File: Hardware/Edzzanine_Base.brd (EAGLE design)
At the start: 30.5 x 44.5 mm, 6 parts

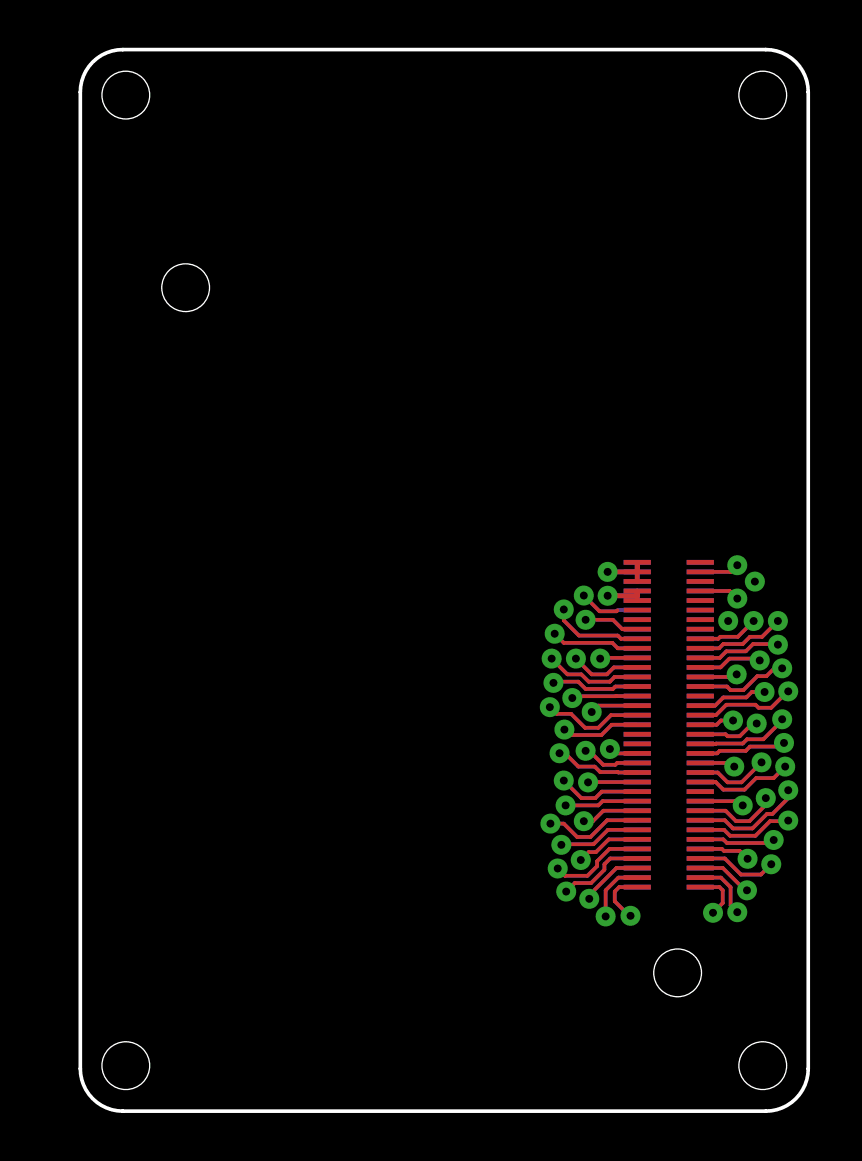
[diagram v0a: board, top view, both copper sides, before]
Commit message: completed base layout, ready for review.  Removed testing layouts and other noise
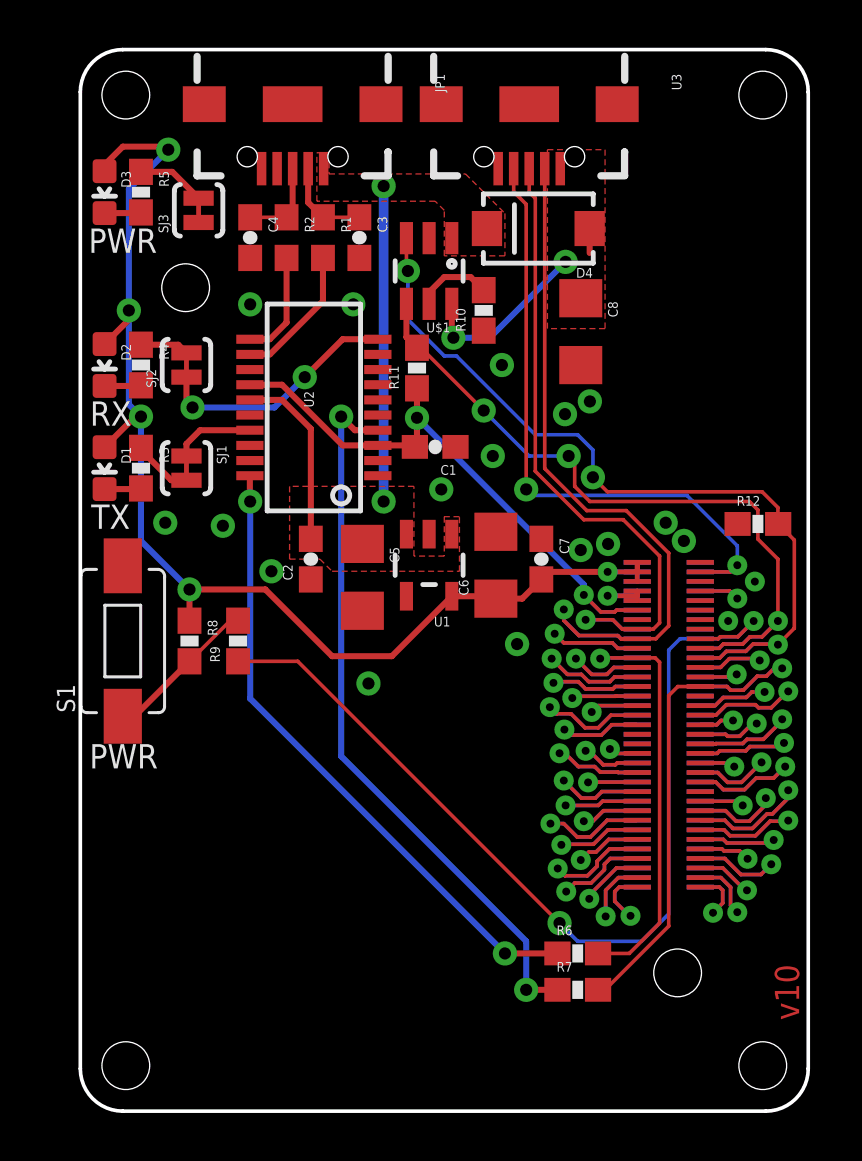
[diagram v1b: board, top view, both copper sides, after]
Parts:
- added C1, C2, C7: 0.1uF, SparkFun-Capacitors:0603-CAP
- added C3, C4: 47pF, SparkFun-Capacitors:0603-CAP
- added C5, C6, C8: 10uF, SparkFun-Capacitors:1206
- added D1: RED, SparkFun-LED:LED-0603
- added D2: YELLOW, SparkFun-LED:LED-0603
- added D3: BLUE, SparkFun-LED:LED-0603
- added D4: (no value), SparkFun-DiscreteSemi:SMA-DIODE
- added JP1: USB_MICROB, SparkFun-Connectors:USB-B-MICRO-SMD_V03
- added R1, R2: 27, SparkFun-Resistors:0603
- added R10: 287, SparkFun-Resistors:0603-RES
- added R11, R8: 10K, SparkFun-Resistors:0603-RES
- added R12: 100k, SparkFun-Resistors:0603-RES
- added R3, R4, R5: 1K, SparkFun-Resistors:0603-RES
- added R6, R7: 100, SparkFun-Resistors:0603-RES
- added R9: 22, SparkFun-Resistors:0603-RES
- added S1: POWER, SparkFun-Electromechanical:TACTILE-SWITCH-1101NE
- added SJ1, SJ2, SJ3: JUMPER-PAD-2-NC_BY_TRACE, SparkFun-Passives:PAD-JUMPER-2-NC_BY_TRACE_YES_SILK
- added U$1: MIC2039, Testing:SOT23-6
- added U1: MIC5219 3.3V, SparkFun-PowerIC:SOT23-5
- added U2: FTS31XS-U, SparkFun-DigitalIC:SSOP20_L
- added U3: (no value), SparkFun-Connectors:USB-AB-MICRO-SMD_V03
- renumbered U$2 to E1
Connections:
- new net 5V: C2.2, C5.1, D4.C, JP1.VBUS1, U$1.1, U1.1, U1.3, U2.15
- new net N$1: SJ1.1, U2.17
- new net N$10: D2.C, R4.2
- new net N$11: R6.1, U2.20
- new net N$12: D3.C, R5.2
- new net N$13: R5.1, SJ3.2
- new net N$14: R7.1, U2.4
- new net N$15: R8.2, R9.2, S1.P$1
- new net N$16: R10.2, U$1.5
- new net N$18: C8.1, D4.A, U$1.6, U3.VBUS1
- new net N$2: C3.1, JP1.D-1, R1.1
- new net N$3: C4.1, JP1.D+1, R2.1
- new net N$4: R1.2, U2.12
- new net N$5: R2.2, U2.11
- new net N$6: SJ2.1, U2.10
- new net N$7: R3.1, SJ1.2
- new net N$8: R4.1, SJ2.2
- new net N$9: D1.C, R3.2
- net 1.8V: now also C1.2, R11.1, U2.14, U2.3
- net FAULT: now also R11.2, U$1.4
- net GND: now also C1.1, C2.1, C3.2, C4.2, C5.2, C6.2, C7.1, C8.2, JP1.GND1, JP1.SHIELD1, JP1.SHIELD2, JP1.SHIELD3, R10.1, R12.1, S1.P$2, SJ3.1, U$1.2, U1.2, U2.16, U2.6, U3.GND1
- net GP134_UART_2_RX: now also R6.2
- net GP135_UART_2_TX: now also R7.2
- net PSW: now also R12.2, U$1.3
- net PWRBTN#: now also R9.1
- net USB_DN: now also U3.D-1
- net USB_DP: now also U3.D+1
- net USB_ID: now also U3.ID1
- net VSYS: now also C6.1, C7.2, D1.A, D2.A, D3.A, R8.1, U1.5
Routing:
- net VSYS: track 4.48 -> 53.3 mm, vias 1 -> 5
- net PWRBTN#: track 5.08 -> 41.3 mm, vias 1 -> 2
- net N$14: track 0.00 -> 30.3 mm, vias 0 -> 2
- net PSW: track 7.00 -> 36.2 mm, vias 1 -> 3
- net N$11: track 0.00 -> 26.6 mm, vias 0 -> 2
- net FAULT: track 7.45 -> 32.1 mm, vias 1 -> 3
- net USB_ID: track 3.33 -> 27.6 mm, vias 1 -> 2
- net USB_DN: track 7.70 -> 31.5 mm
- net USB_DP: track 4.65 -> 27.9 mm
- net 1.8V: track 4.25 -> 25.9 mm, vias 1 -> 2
- net 5V: track 0.00 -> 20.9 mm, vias 0 -> 2
- net GP135_UART_2_TX: track 7.74 -> 22.9 mm
- net GP134_UART_2_RX: track 3.13 -> 18.2 mm
- net N$6: track 0.00 -> 10.3 mm, vias 0 -> 2
- net N$18: track 0.00 -> 8.49 mm, vias 0 -> 2
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- added copper zone on layer 1, net 5V
- added copper zone on layer 1, net N$18
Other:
- board text added: "CONSOLE"
- board text added: "Edizzine Console"
- board text added: "OTG"
- board text added: "PWR"
- board text added: "RX"
- board text added: "TX"
- board text added: "v10"
- board text removed: "Example Name of Board"
